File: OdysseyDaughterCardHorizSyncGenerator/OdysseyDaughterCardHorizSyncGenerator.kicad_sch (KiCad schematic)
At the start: 16 parts, among them Q1 BC547B, Q2 BC556B, Q3 2N3904, X1 OdysseyDaughterCard

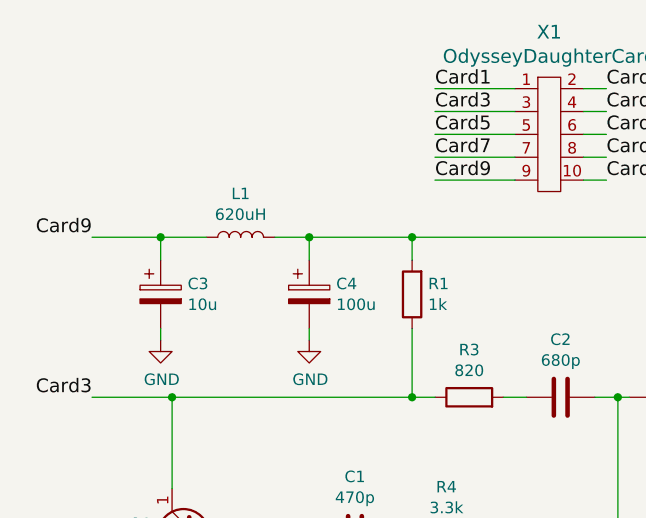
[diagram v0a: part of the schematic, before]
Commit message: OdysseyDaughterCardHorizSyncGenerator wider transistor footprint, add logo, generate pdf, images, 3d models
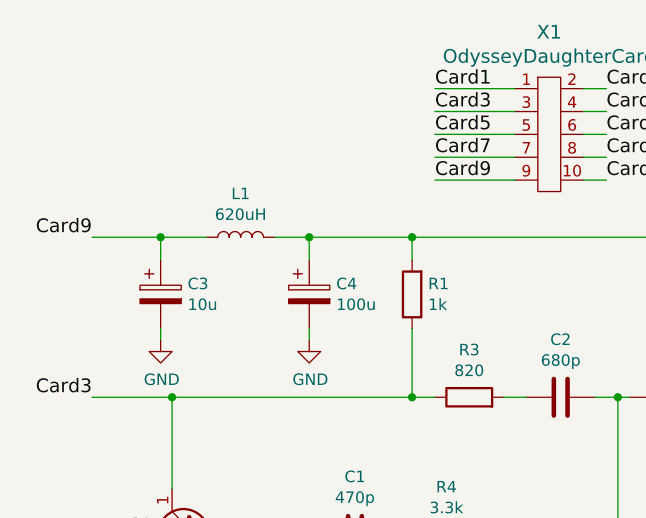
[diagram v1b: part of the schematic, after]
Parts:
- Q1, Q2, Q3: footprint Package_TO_SOT_THT:TO-92_Inline -> Package_TO_SOT_THT:TO-92_Inline_Wide
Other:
- company: University of Pittsburgh - Odyssey Restoration Project -> University of Pittsburgh - OdysseyNow
